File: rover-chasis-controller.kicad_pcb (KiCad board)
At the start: 2 copper layers, 86 x 97 mm, 82 parts, among them J1 Motor control, J11 Compass Connection (I2C), J15 External LED (Red), J16 External LED (Yellow), J17 External LED (Green), J2 Motor control, J22 Ultrasonic Sensor Inputs, J3 Motor control, J38 Motor control, J4 Screw_Terminal_01x02, J40 Encoder, J41 Encoder, J42 Encoder, J43 Encoder, J7 TTL, J8 Ultrasonic Sensor Inputs, Q14 MMBT3904_C181119, Q2 HSBA100P04_C2987717, Q33 MMBT3904_C181119, Q34 MMBT3904_C181119, Q35 MMBT3904_C181119, U1 APT2012LVBC/D, U2 APT2012LVBC/D, U3 APT2012LVBC/D, U4 AP64500, U5 MPU-6050_C24112, U6 PCA9685PW,118, U7 APT2012LVBC/D

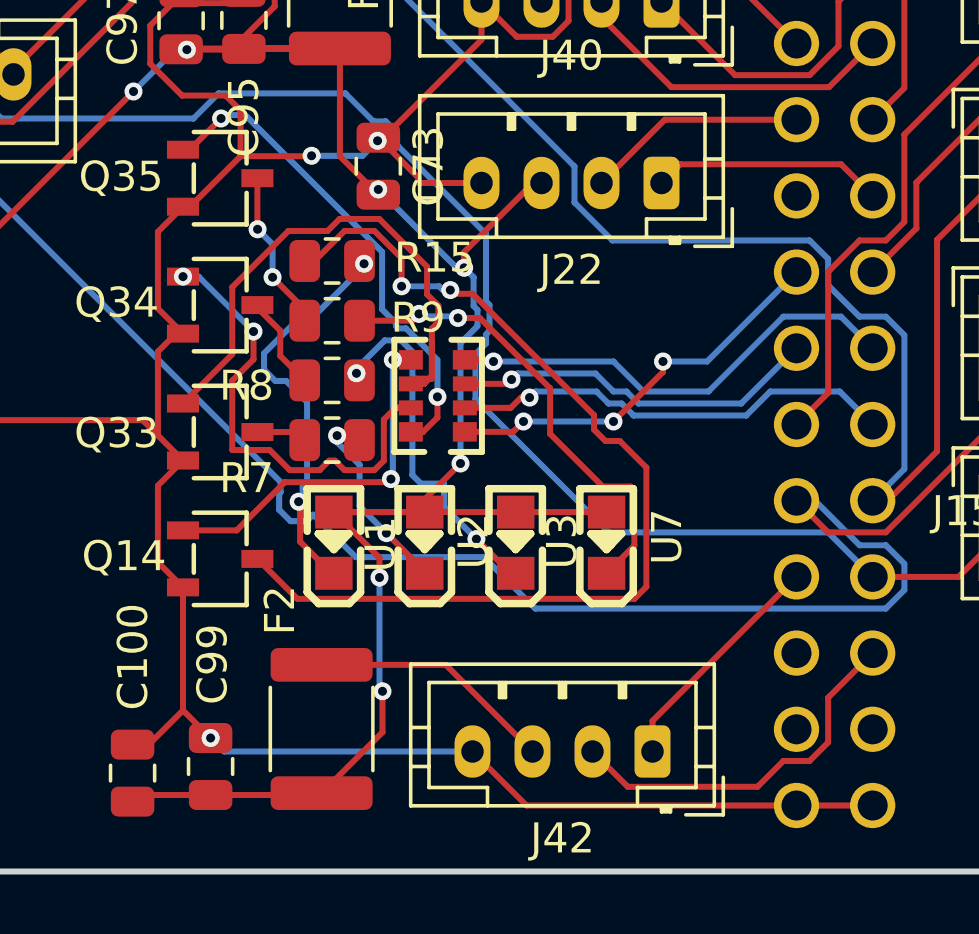
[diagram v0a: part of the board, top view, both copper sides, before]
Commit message: Issue #1: Replaced out-of-stock components
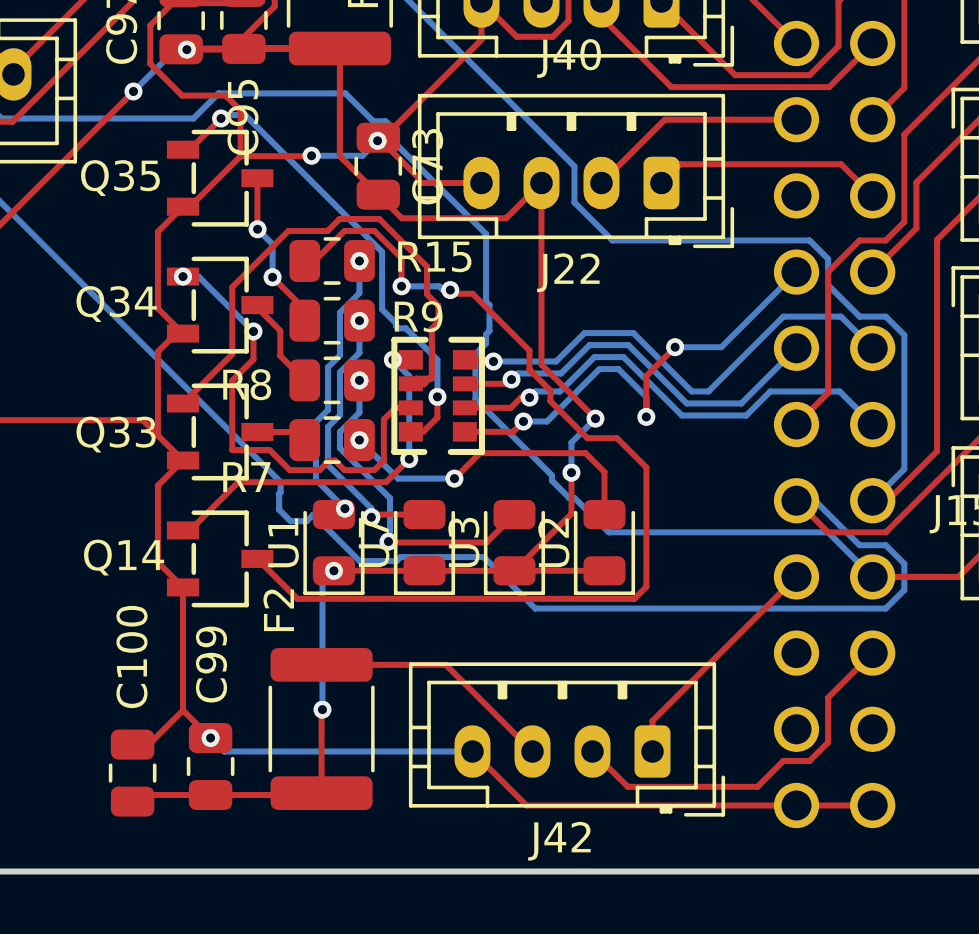
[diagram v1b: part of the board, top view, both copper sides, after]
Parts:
- U1, U2, U3, U7: footprint easyeda2kicad:LED-SMD_L2.0-W1.3-R-RD -> LED_SMD:LED_0805_2012Metric
- moved U7 6.07 mm to (86.0, 129.1)
- moved U2 5.99 mm to (92.0, 129.1)
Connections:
- U4 pad EPAD: GND -> (no net)
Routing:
- net Net-(U7-K): track 15.7 -> 9.39 mm
- net Net-(U2-K): track 5.80 -> 10.7 mm
- net Net-(U1-K): track 14.1 -> 9.71 mm
- net /LED_BLUE_4: track 13.5 -> 15.8 mm
- net VCC (5V): track 235.0 -> 232.9 mm, vias 19 -> 18
- net Net-(U3-K): track 11.9 -> 11.0 mm
- net /LED_BLUE_3: track 14.9 -> 15.9 mm
- net /LED_BLUE_1: track 15.5 -> 16.3 mm
- net /LED_BLUE_2: track 12.4 -> 13.2 mm
